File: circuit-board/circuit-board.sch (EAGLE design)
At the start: 51 parts, among them IC1 UA78M05DCY, Q1 BC547B, Q2 BC547B, U1 MAX3232, U2 ATMEGA328P, U3 ADUM1201BRZ, Y2 16MHz

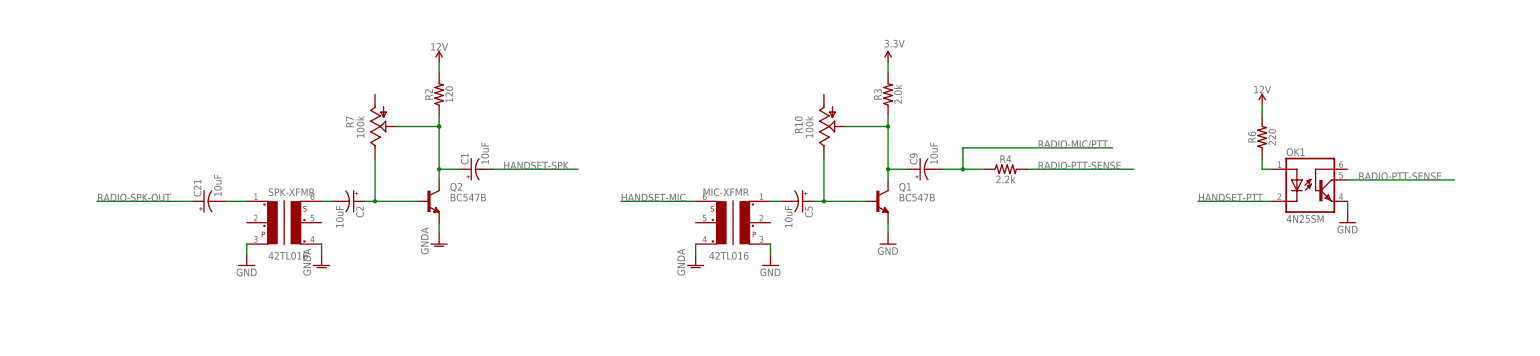
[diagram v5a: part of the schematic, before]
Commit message: Tweak some resistor values in V2 board based on breadboard testing.  Add small input resistors on both amplifying transistors -- this cleans up the mic signal a lot!
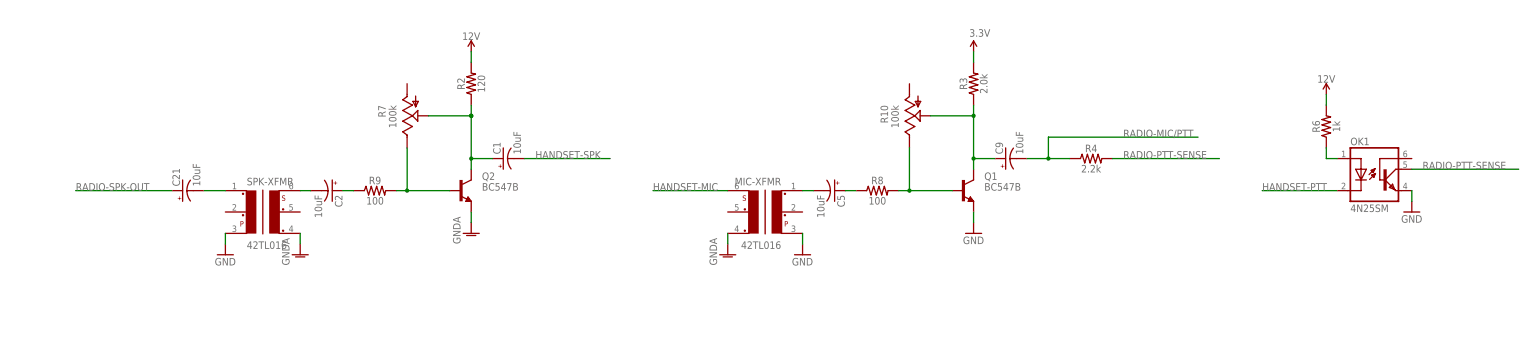
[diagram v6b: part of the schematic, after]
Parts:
- added R8, R9: 100, SparkFun-Resistors:100OHM-0603-1/10W-1%
- R6: value 220 -> 1k; device SparkFun-Resistors:220OHM-0603-1/10W-1% -> SparkFun-Resistors:1KOHM-0603-1/10W-1%
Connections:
- new net N$10: C2.+, R9.1
- new net N$8: C5.+, R8.1
- net N$4: now also R8.2; no longer C5.+
- net N$5: now also R9.2; no longer C2.+
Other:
- moved on the sheet: C1, C2, C21, C5, C9, MIC-XFMR, OK1, Q1, Q2, R10, R2, R3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

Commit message: Switched 100/120 ohm resistors in audio amp circuit for 1k resistors -- noise almost eliminated, though serial noise remains.. will need to split up ground planes to clear that up
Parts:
- R2: value 120 -> 1k; device SparkFun-Resistors:RESISTOR0603 -> SparkFun-Resistors:1KOHM-0603-1/10W-1%
- R8, R9: value 100 -> 1k; device SparkFun-Resistors:100OHM-0603-1/10W-1% -> SparkFun-Resistors:1KOHM-0603-1/10W-1%

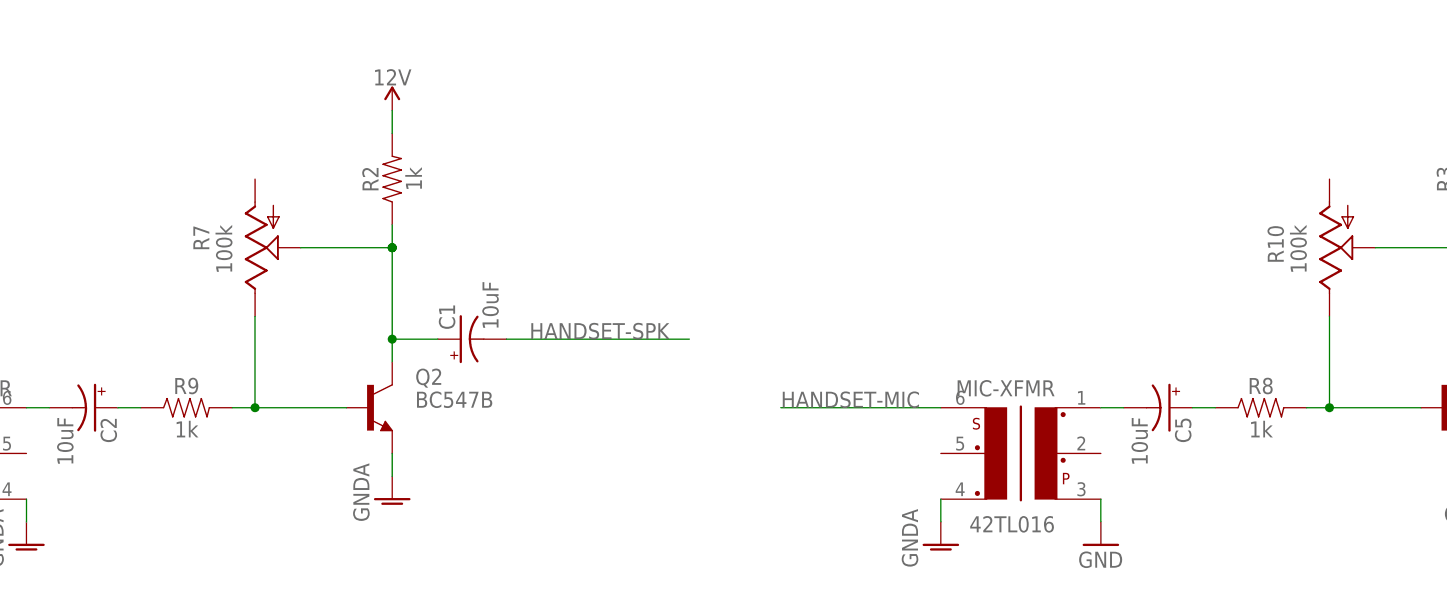
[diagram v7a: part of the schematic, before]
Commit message: Updated resistor values on adapter board to be consistent with what I ended up building
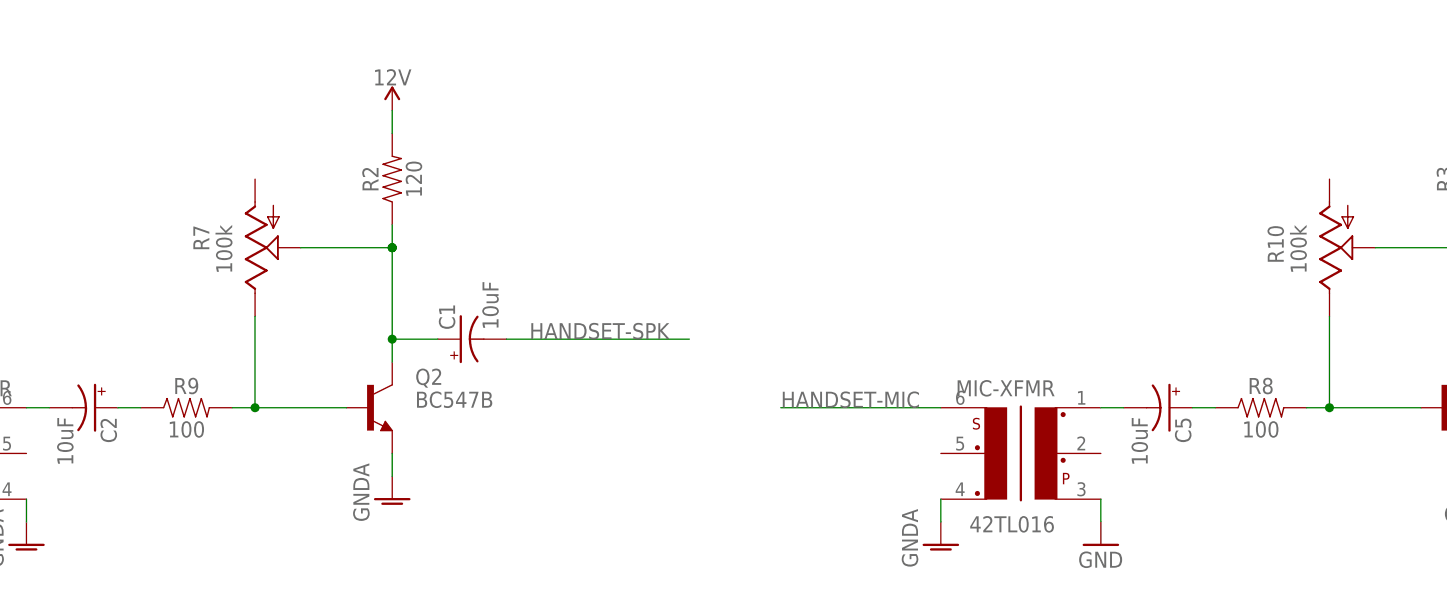
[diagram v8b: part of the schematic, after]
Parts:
- R2: value 1k -> 120; device SparkFun-Resistors:1KOHM-0603-1/10W-1% -> SparkFun-Resistors:RESISTOR0603
- R8, R9: value 1k -> 100; device SparkFun-Resistors:1KOHM-0603-1/10W-1% -> SparkFun-Resistors:100OHM-0603-1/4W-5%
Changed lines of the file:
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@@
 <part name="GND25" library="supply1" deviceset="GND" device=""/>
 <part name="SPK-XFMR" library="trafo-xicon" library_urn="urn:adsk.eagle:library:393" deviceset="42T?*" device="L" package3d_urn="urn:adsk.eagle:package:28185/1" technology="016"/>
-<part name="R2" library="SparkFun-Resistors" library_urn="urn:adsk.eagle:library:532" deviceset="1KOHM" device="-0603-1/10W-1%" package3d_urn="urn:adsk.eagle:package:39650/1" value="1k"/>
+<part name="R2" library="SparkFun-Resistors" library_urn="urn:adsk.eagle:library:532" deviceset="RESISTOR" device="0603" package3d_urn="urn:adsk.eagle:package:39650/1" value="120"/>
 <part name="Y2" library="SparkFun-Clocks" library_urn="urn:adsk.eagle:library:511" deviceset="CRYSTAL-GROUNDED" device="SMD-3.2X2.5" package3d_urn="urn:adsk.eagle:package:37521/1" value="16MHz"/>
 <part name="GND24" library="supply1" deviceset="GNDA" device=""/>
@@
 <part name="GND7" library="supply1" deviceset="GNDA" device=""/>
 <part name="R6" library="SparkFun-Resistors" library_urn="urn:adsk.eagle:library:532" deviceset="1KOHM" device="-0603-1/10W-1%" package3d_urn="urn:adsk.eagle:package:39650/1" value="1k"/>
-<part name="R8" library="SparkFun-Resistors" library_urn="urn:adsk.eagle:library:532" deviceset="1KOHM" device="-0603-1/10W-1%" package3d_urn="urn:adsk.eagle:package:39650/1" value="1k"/>
-<part name="R9" library="SparkFun-Resistors" library_urn="urn:adsk.eagle:library:532" deviceset="1KOHM" device="-0603-1/10W-1%" package3d_urn="urn:adsk.eagle:package:39650/1" value="1k"/>
+<part name="R8" library="SparkFun-Resistors" library_urn="urn:adsk.eagle:library:532" deviceset="100OHM" device="-0603-1/4W-5%" package3d_urn="urn:adsk.eagle:package:39650/1" value="100"/>
+<part name="R9" library="SparkFun-Resistors" library_urn="urn:adsk.eagle:library:532" deviceset="100OHM" device="-0603-1/4W-5%" package3d_urn="urn:adsk.eagle:package:39650/1" value="100"/>
 </parts>
 <sheets>
